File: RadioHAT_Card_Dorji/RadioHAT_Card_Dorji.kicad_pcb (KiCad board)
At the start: 2 copper layers, 30 x 51 mm, 10 parts, among them J2 Conn_Coaxial, J3 Conn_Coaxial, J4 Conn_Coaxial, J5 Conn_Coaxial, J6 Conn_Coaxial

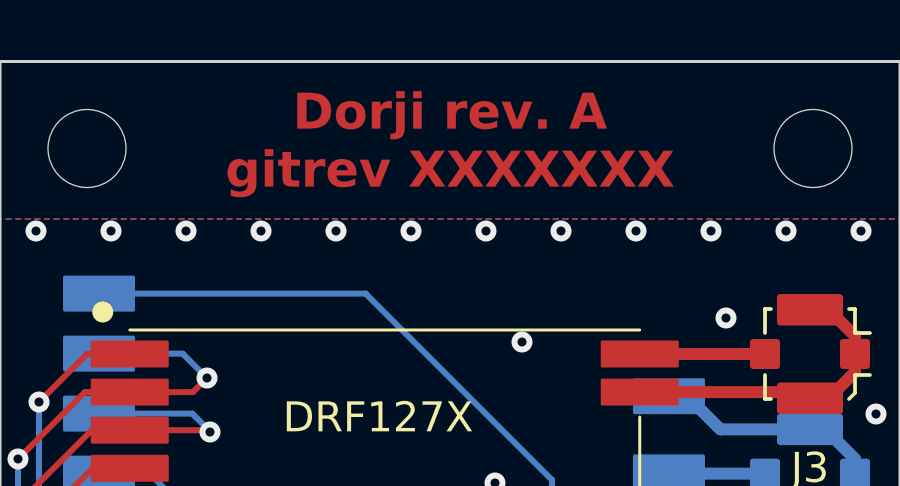
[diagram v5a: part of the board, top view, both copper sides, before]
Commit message: [PCB] Add git hash tag for CI
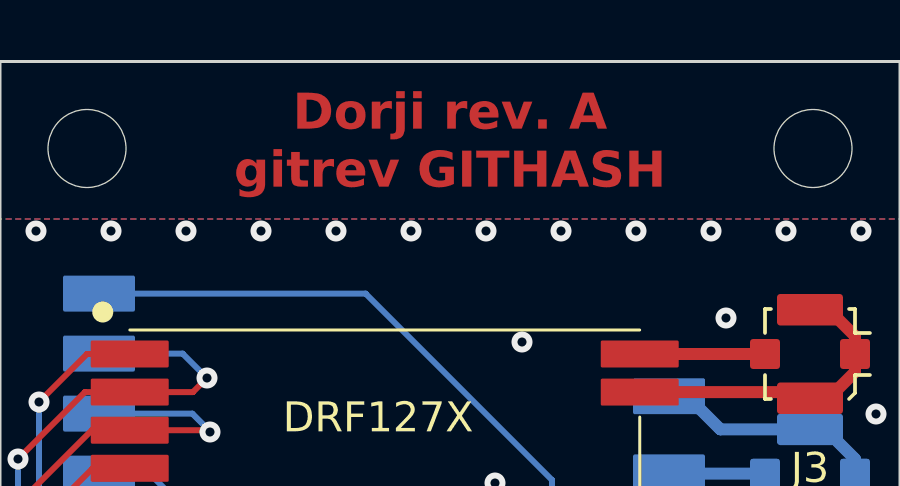
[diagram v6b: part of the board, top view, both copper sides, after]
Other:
- board text added: "Dorji rev. A gitrev GITHASH"
- board text removed: "Dorji rev. A gitrev XXXXXXX"
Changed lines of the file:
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@@
 		)
 	)
-	(gr_text "Dorji rev. A\ngitrev XXXXXXX"
+	(gr_text "Dorji rev. A\ngitrev GITHASH"
 		(at 132.8 71.7 0)
 		(layer "F.Cu")
